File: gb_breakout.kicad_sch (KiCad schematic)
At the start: 13 parts, among them J1 Conn_02x16_Counter_Clockwise, U1 Cartridge_Bus

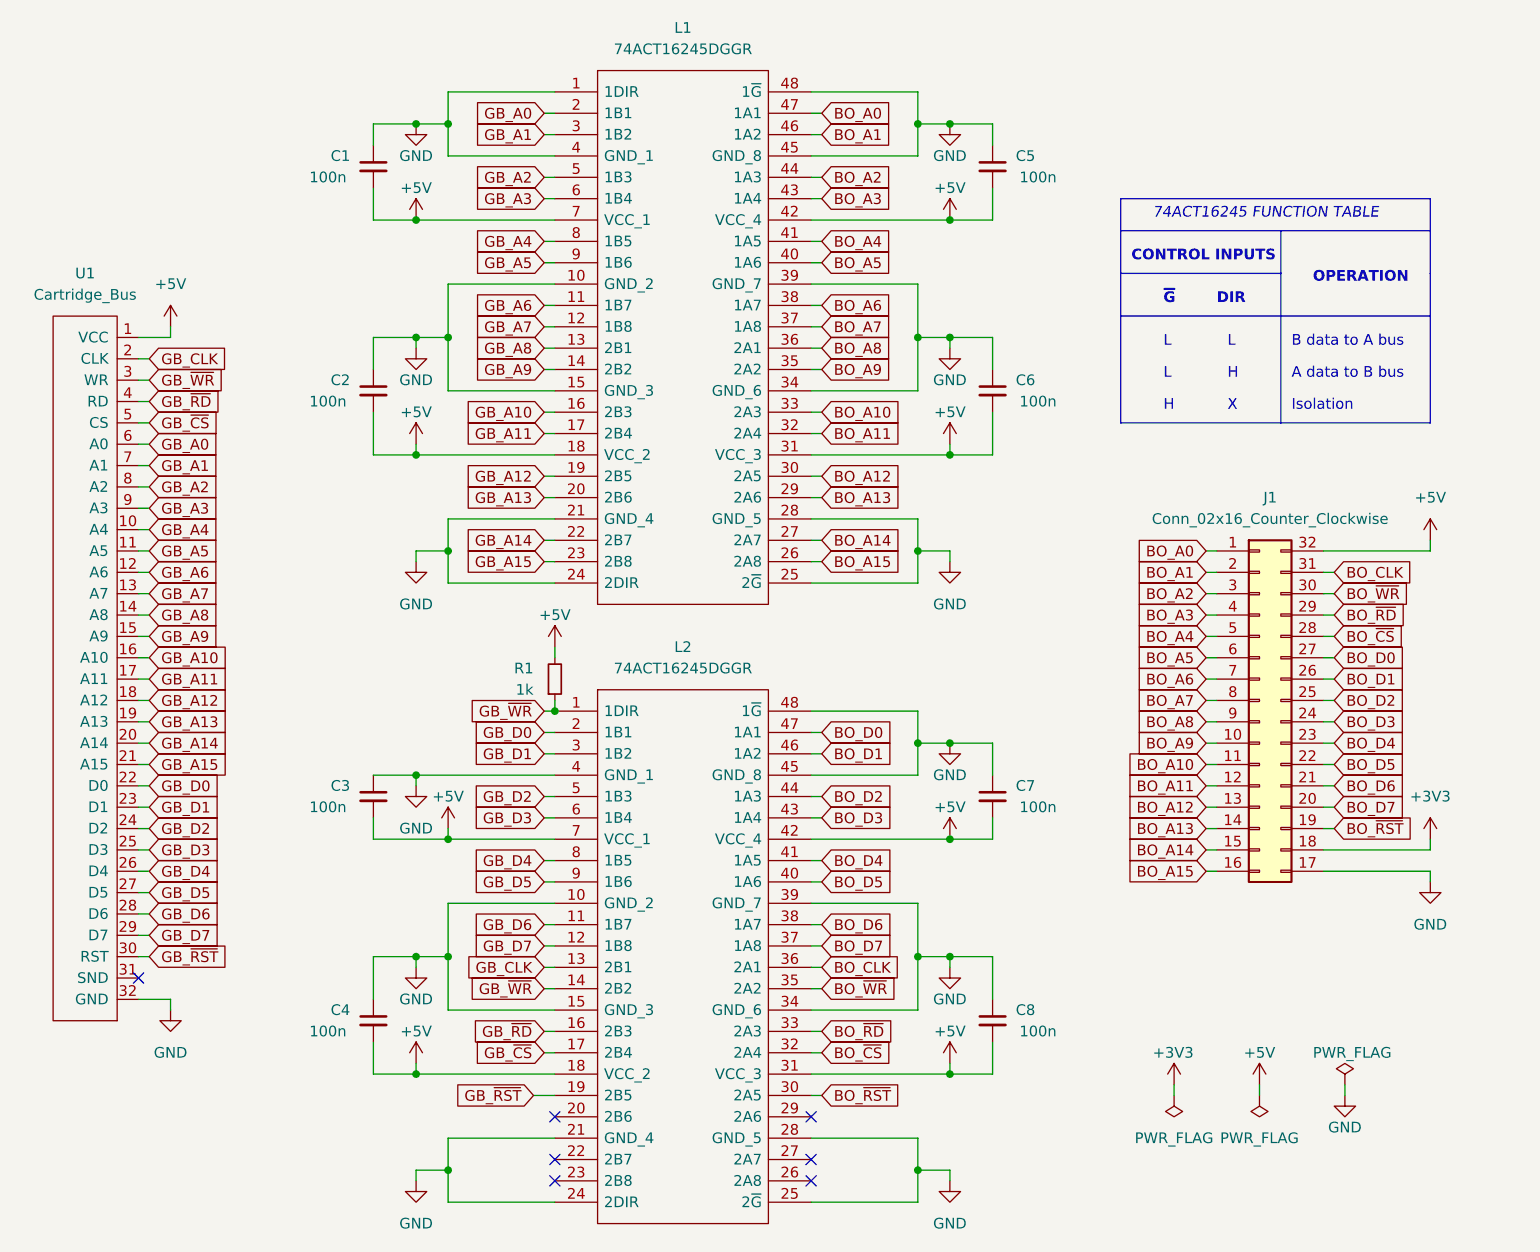
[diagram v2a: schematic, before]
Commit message: switched to 74ALVC164245 for level shifting
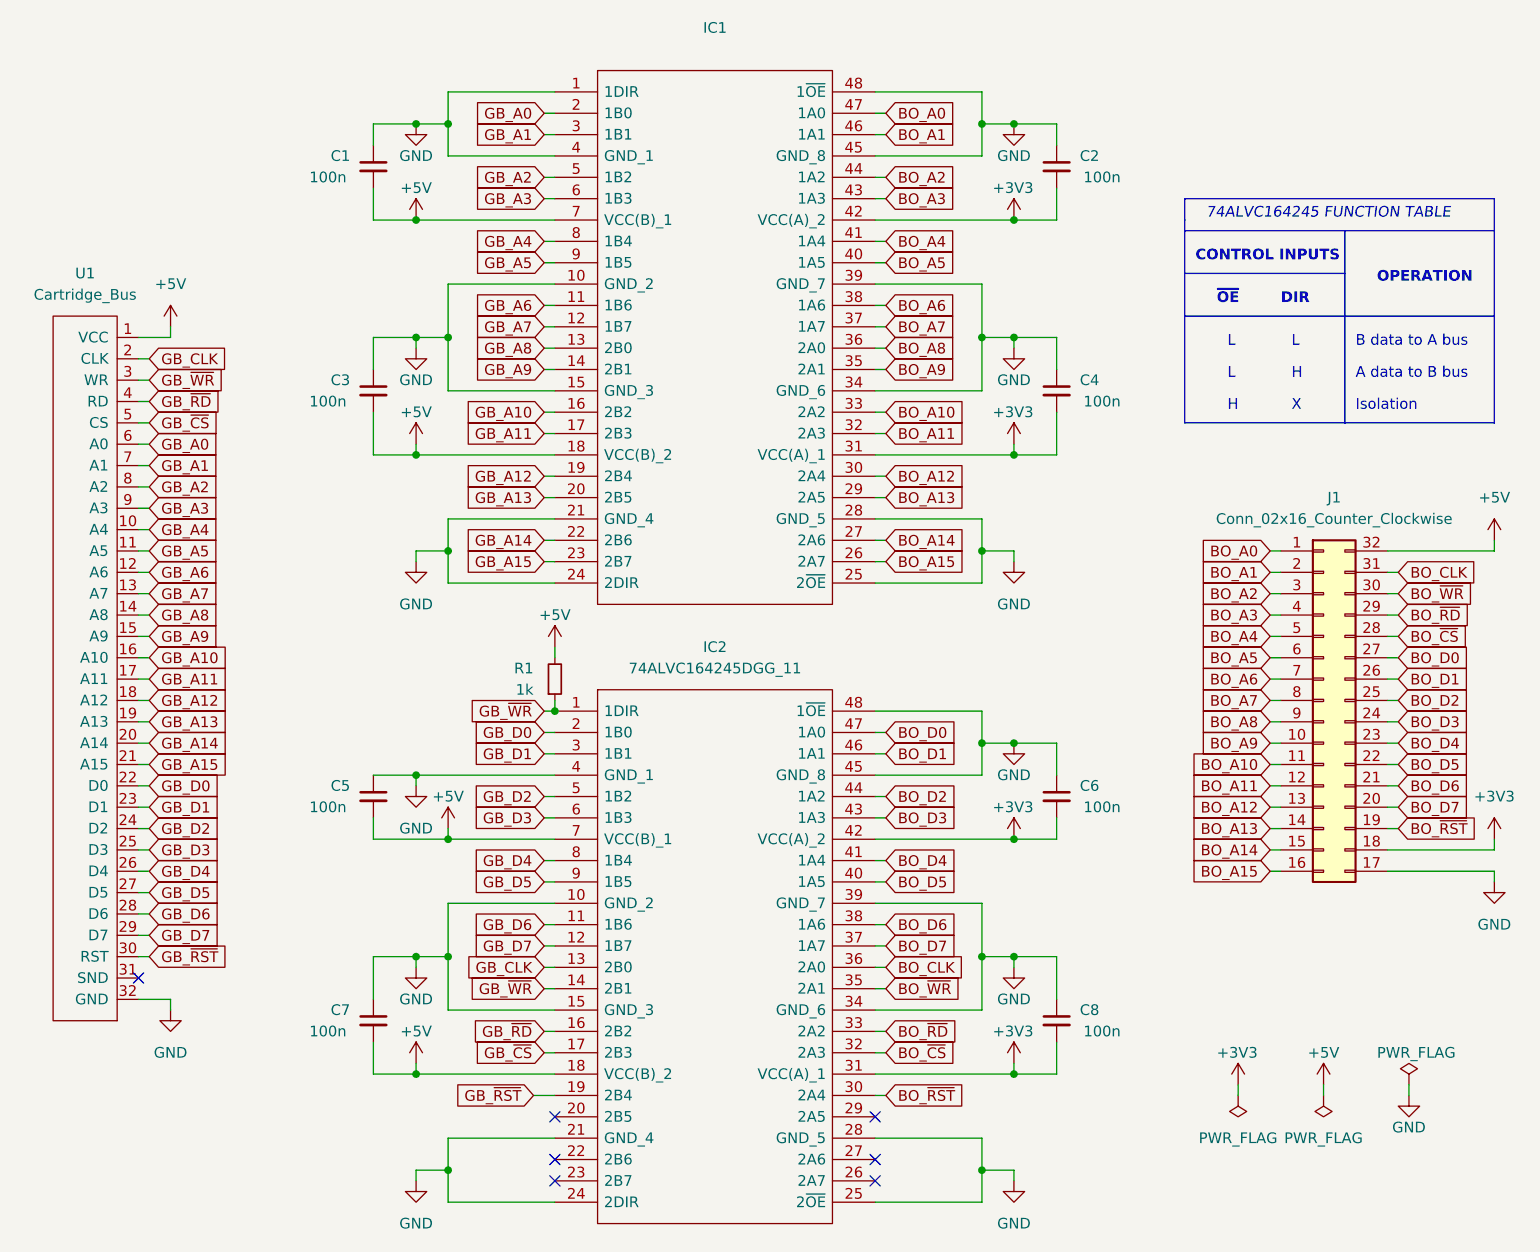
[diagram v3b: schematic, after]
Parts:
- removed L1, L2: 74ACT16245DGGR, 74ACT16245DGGR:SOP50P810X120-48N, symbol 74ACT16245DGGR:74ACT16245DGGR
- added IC1: (no value), symbol 74ALVC164245DGG_11:74ALVC164245DGG_11
- added IC2: 74ALVC164245DGG_11, symbol 74ALVC164245DGG_11:74ALVC164245DGG_11
- renumbered C5 to C2, C2 to C3, C6 to C4, C3 to C5, C7 to C6, C4 to C7
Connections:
- net +3V3: now also C2.2, C4.2, C6.2, C8.2, IC1.31 (VCC(A)_1), IC1.42 (VCC(A)_2), IC2.31 (VCC(A)_1), IC2.42 (VCC(A)_2)
- net +5V: now also IC1.18 (VCC(B)_2), IC1.7 (VCC(B)_1), IC2.18 (VCC(B)_2), IC2.7 (VCC(B)_1); no longer C2.2, C4.2, C6.2, C8.2
- net BO_A0: now also IC1.47 (1A0)
- net BO_A1: now also IC1.46 (1A1)
- net BO_A10: now also IC1.33 (2A2)
- net BO_A11: now also IC1.32 (2A3)
- net BO_A12: now also IC1.30 (2A4)
- net BO_A13: now also IC1.29 (2A5)
- net BO_A14: now also IC1.27 (2A6)
- net BO_A15: now also IC1.26 (2A7)
- net BO_A2: now also IC1.44 (1A2)
- net BO_A3: now also IC1.43 (1A3)
- net BO_A4: now also IC1.41 (1A4)
- net BO_A5: now also IC1.40 (1A5)
- net BO_A6: now also IC1.38 (1A6)
- net BO_A7: now also IC1.37 (1A7)
- net BO_A8: now also IC1.36 (2A0)
- net BO_A9: now also IC1.35 (2A1)
- net BO_CLK: now also IC2.36 (2A0)
- net BO_D0: now also IC2.47 (1A0)
- net BO_D1: now also IC2.46 (1A1)
- net BO_D2: now also IC2.44 (1A2)
- net BO_D3: now also IC2.43 (1A3)
- net BO_D4: now also IC2.41 (1A4)
- net BO_D5: now also IC2.40 (1A5)
- net BO_D6: now also IC2.38 (1A6)
- net BO_D7: now also IC2.37 (1A7)
- net BO_~{CS}: now also IC2.32 (2A3)
- net BO_~{RD}: now also IC2.33 (2A2)
- net BO_~{RST}: now also IC2.30 (2A4)
- net BO_~{WR}: now also IC2.35 (2A1)
- net GB_A0: now also IC1.2 (1B0)
- net GB_A1: now also IC1.3 (1B1)
- net GB_A10: now also IC1.16 (2B2)
- net GB_A11: now also IC1.17 (2B3)
- net GB_A12: now also IC1.19 (2B4)
- net GB_A13: now also IC1.20 (2B5)
- net GB_A14: now also IC1.22 (2B6)
- net GB_A15: now also IC1.23 (2B7)
- net GB_A2: now also IC1.5 (1B2)
- net GB_A3: now also IC1.6 (1B3)
- net GB_A4: now also IC1.8 (1B4)
- net GB_A5: now also IC1.9 (1B5)
- net GB_A6: now also IC1.11 (1B6)
- net GB_A7: now also IC1.12 (1B7)
- net GB_A8: now also IC1.13 (2B0)
- net GB_A9: now also IC1.14 (2B1)
- net GB_CLK: now also IC2.13 (2B0)
- net GB_D0: now also IC2.2 (1B0)
- net GB_D1: now also IC2.3 (1B1)
- net GB_D2: now also IC2.5 (1B2)
- net GB_D3: now also IC2.6 (1B3)
- net GB_D4: now also IC2.8 (1B4)
- net GB_D5: now also IC2.9 (1B5)
- net GB_D6: now also IC2.11 (1B6)
- net GB_D7: now also IC2.12 (1B7)
- net GB_~{CS}: now also IC2.17 (2B3)
- net GB_~{RD}: now also IC2.16 (2B2)
- net GB_~{RST}: now also IC2.19 (2B4)
- net GB_~{WR}: now also IC2.1 (1DIR), IC2.14 (2B1)
- net GND: now also IC1.1 (1DIR), IC1.10 (GND_2), IC1.15 (GND_3), IC1.21 (GND_4), IC1.24 (2DIR), IC1.25 (2~{OE}), IC1.28 (GND_5), IC1.34 (GND_6), IC1.39 (GND_7), IC1.4 (GND_1), IC1.45 (GND_8), IC1.48 (1~{OE}), IC2.10 (GND_2), IC2.15 (GND_3), IC2.21 (GND_4), IC2.24 (2DIR), IC2.25 (2~{OE}), IC2.28 (GND_5), IC2.34 (GND_6), IC2.39 (GND_7), IC2.4 (GND_1), IC2.45 (GND_8), IC2.48 (1~{OE})
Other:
- note added: "74ALVC164245 FUNCTION TABLE"
- note added: "~{OE}"
- note removed: "74ACT16245 FUNCTION TABLE"
- note removed: "~{G}"
- moved on the sheet: C2, C4, C6, C8, J1

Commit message: finish routing address lines, start routing data lines
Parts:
- IC1: value (none) -> 74ALVC164245DGG_11; footprint (none) -> 74ALVC164245DGG_11:SOP50P810X120-48N
- IC2: footprint (none) -> 74ALVC164245DGG_11:SOP50P810X120-48N
- U1: value Cartridge_Bus -> (none); footprint HDR_Gameboy_Cartridges:GB_Cartridge -> (none)
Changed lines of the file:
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@@
     (in_bom yes) (on_board yes) (fields_autoplaced)
     (property "Reference" "IC1" (id 0) (at 135.89 16.51 0))
-    (property "Value" "" (id 1) (at 135.89 19.05 0))
-    (property "Footprint" "" (id 2) (at 151.13 21.59 0)
+    (property "Value" "74ALVC164245DGG_11" (id 1) (at 135.89 19.05 0))
+    (property "Footprint" "74ALVC164245DGG_11:SOP50P810X120-48N" (id 2) (at 151.13 21.59 0)
       (effects (font (size 1.27 1.27)) (justify left) hide)
     )
@@
     (property "Reference" "IC2" (id 0) (at 135.89 90.17 0))
     (property "Value" "74ALVC164245DGG_11" (id 1) (at 135.89 92.71 0))
-    (property "Footprint" "" (id 2) (at 151.13 95.25 0)
+    (property "Footprint" "74ALVC164245DGG_11:SOP50P810X120-48N" (id 2) (at 151.13 95.25 0)
       (effects (font (size 1.27 1.27)) (justify left) hide)
     )
@@
     (in_bom yes) (on_board yes) (fields_autoplaced)
     (property "Reference" "U1" (id 0) (at 60.96 45.72 90))
-    (property "Value" "Cartridge_Bus" (id 1) (at 60.96 48.26 90))
-    (property "Footprint" "HDR_Gameboy_Cartridges:GB_Cartridge" (id 2) (at 64.77 68.58 0)
+    (property "Value" "" (id 1) (at 60.96 48.26 90))
+    (property "Footprint" "" (id 2) (at 64.77 68.58 0)
       (effects (font (size 1.27 1.27)) hide)
     )
@@
       (reference "R1") (unit 1) (value "1k") (footprint "Resistor_SMD:R_0201_0603Metric")
     )
-    (path "/85255a37-874d-44ab-bbc7-86e671be0f3c"
+    (path "/8445dacb-1773-4653-87d7-55d6d433fe85"
       (reference "U1") (unit 1) (value "Cartridge_Bus") (footprint "HDR_Gameboy_Cartridges:GB_Cartridge")
     )

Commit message: switch decoupling caps to imperial 0603
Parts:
- C1, C2, C3, C4, C5, C6, C7, C8: footprint Capacitor_SMD:C_0201_0603Metric -> (none)
- U1: value (none) -> Cartridge_Bus; footprint (none) -> HDR_Gameboy_Cartridges:GB_Cartridge
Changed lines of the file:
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@@
       (effects (font (size 1.27 1.27)) (justify right))
     )
-    (property "Footprint" "Capacitor_SMD:C_0201_0603Metric" (id 2) (at 95.25 134.62 0)
+    (property "Footprint" "" (id 2) (at 95.25 134.62 0)
       (effects (font (size 1.27 1.27)) hide)
     )
@@
     (in_bom yes) (on_board yes) (fields_autoplaced)
     (property "Reference" "U1" (id 0) (at 60.96 45.72 90))
-    (property "Value" "" (id 1) (at 60.96 48.26 90))
-    (property "Footprint" "" (id 2) (at 64.77 68.58 0)
+    (property "Value" "Cartridge_Bus" (id 1) (at 60.96 48.26 90))
+    (property "Footprint" "HDR_Gameboy_Cartridges:GB_Cartridge" (id 2) (at 64.77 68.58 0)
       (effects (font (size 1.27 1.27)) hide)
     )
@@
       (effects (font (size 1.27 1.27)) (justify right))
     )
-    (property "Footprint" "Capacitor_SMD:C_0201_0603Metric" (id 2) (at 176.53 107.95 0)
+    (property "Footprint" "" (id 2) (at 176.53 107.95 0)
       (effects (font (size 1.27 1.27)) hide)
     )
@@
       (effects (font (size 1.27 1.27)) (justify right))
     )
-    (property "Footprint" "Capacitor_SMD:C_0201_0603Metric" (id 2) (at 95.25 33.02 0)
+    (property "Footprint" "" (id 2) (at 95.25 33.02 0)
       (effects (font (size 1.27 1.27)) hide)
     )
@@
       (effects (font (size 1.27 1.27)) (justify right))
     )
-    (property "Footprint" "Capacitor_SMD:C_0201_0603Metric" (id 2) (at 176.53 33.02 0)
+    (property "Footprint" "" (id 2) (at 176.53 33.02 0)
       (effects (font (size 1.27 1.27)) hide)
     )
@@
       (effects (font (size 1.27 1.27)) (justify right))
     )
-    (property "Footprint" "Capacitor_SMD:C_0201_0603Metric" (id 2) (at 95.25 107.95 0)
+    (property "Footprint" "" (id 2) (at 95.25 107.95 0)
       (effects (font (size 1.27 1.27)) hide)
     )
@@
       (effects (font (size 1.27 1.27)) (justify right))
     )
-    (property "Footprint" "Capacitor_SMD:C_0201_0603Metric" (id 2) (at 95.25 59.69 0)
+    (property "Footprint" "" (id 2) (at 95.25 59.69 0)
       (effects (font (size 1.27 1.27)) hide)
     )
@@
       (effects (font (size 1.27 1.27)) (justify right))
     )
-    (property "Footprint" "Capacitor_SMD:C_0201_0603Metric" (id 2) (at 176.53 134.62 0)
+    (property "Footprint" "" (id 2) (at 176.53 134.62 0)
       (effects (font (size 1.27 1.27)) hide)
     )
@@
       (effects (font (size 1.27 1.27)) (justify right))
     )
-    (property "Footprint" "Capacitor_SMD:C_0201_0603Metric" (id 2) (at 176.53 59.69 0)
+    (property "Footprint" "" (id 2) (at 176.53 59.69 0)
       (effects (font (size 1.27 1.27)) hide)
     )
@@
     )
     (path "/b28ab19b-bca4-4c48-a58e-b5d9af57f72a"
-      (reference "C1") (unit 1) (value "100n") (footprint "Capacitor_SMD:C_0201_0603Metric")
+      (reference "C1") (unit 1) (value "100n") (footprint "Capacitor_SMD:C_0603_1608Metric")
     )
     (path "/c1c79e97-1af4-44e8-8145-8598afcefda6"
-      (reference "C2") (unit 1) (value "100n") (footprint "Capacitor_SMD:C_0201_0603Metric")
+      (reference "C2") (unit 1) (value "100n") (footprint "Capacitor_SMD:C_0603_1608Metric")
     )
     (path "/d7fdbe9e-1700-4cf5-a245-374cf5c421c4"
-      (reference "C3") (unit 1) (value "100n") (footprint "Capacitor_SMD:C_0201_0603Metric")
+      (reference "C3") (unit 1) (value "100n") (footprint "Capacitor_SMD:C_0603_1608Metric")
     )
     (path "/eaf44118-1c97-4a04-bd08-7f5f3930e3c3"
-      (reference "C4") (unit 1) (value "100n") (footprint "Capacitor_SMD:C_0201_0603Metric")
+      (reference "C4") (unit 1) (value "100n") (footprint "Capacitor_SMD:C_0603_1608Metric")
     )
     (path "/c72ef019-ae6c-480c-92b2-d4acdb88f1b4"
-      (reference "C5") (unit 1) (value "100n") (footprint "Capacitor_SMD:C_0201_0603Metric")
+      (reference "C5") (unit 1) (value "100n") (footprint "Capacitor_SMD:C_0603_1608Metric")
     )
     (path "/a0c04f80-50ce-4686-9cd8-3561acf71cdf"
-      (reference "C6") (unit 1) (value "100n") (footprint "Capacitor_SMD:C_0201_0603Metric")
+      (reference "C6") (unit 1) (value "100n") (footprint "Capacitor_SMD:C_0603_1608Metric")
     )
     (path "/45d4dd6f-89e1-4931-ba6e-054a4fe7705f"
-      (reference "C7") (unit 1) (value "100n") (footprint "Capacitor_SMD:C_0201_0603Metric")
+      (reference "C7") (unit 1) (value "100n") (footprint "Capacitor_SMD:C_0603_1608Metric")
     )
     (path "/e882b0ad-ca30-4e2e-939a-5215cd594475"
-      (reference "C8") (unit 1) (value "100n") (footprint "Capacitor_SMD:C_0201_0603Metric")
+      (reference "C8") (unit 1) (value "100n") (footprint "Capacitor_SMD:C_0603_1608Metric")
     )
     (path "/66868d80-e5fb-48b0-9aba-6c8277e8b027"

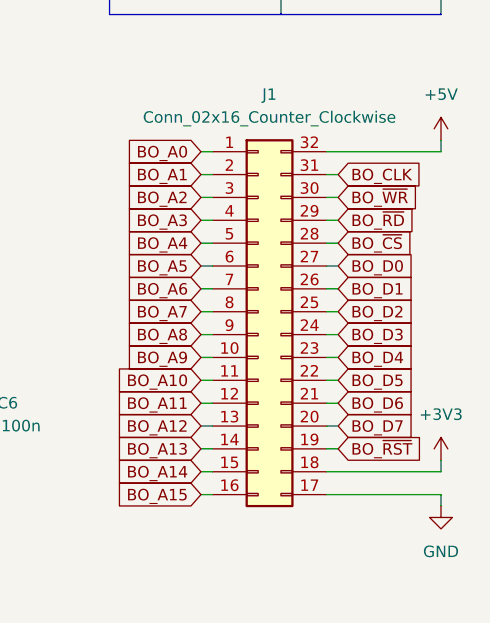
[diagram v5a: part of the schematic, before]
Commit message: fix pin header pinout to make better sense to route
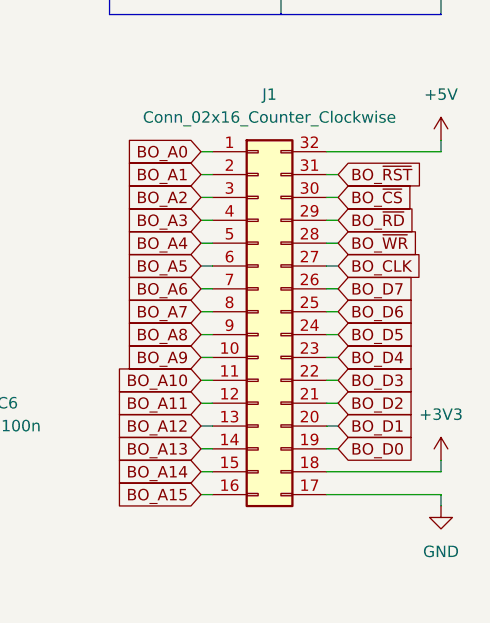
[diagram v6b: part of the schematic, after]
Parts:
- C1, C2, C3, C4, C5, C6, C7, C8: footprint (none) -> Capacitor_SMD:C_0603_1608Metric
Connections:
- net BO_CLK: now also J1.27 (Pin_27); no longer J1.31 (Pin_31)
- net BO_D0: now also J1.19 (Pin_19); no longer J1.27 (Pin_27)
- net BO_D1: now also J1.20 (Pin_20); no longer J1.26 (Pin_26)
- net BO_D2: now also J1.21 (Pin_21); no longer J1.25 (Pin_25)
- net BO_D3: now also J1.22 (Pin_22); no longer J1.24 (Pin_24)
- net BO_D5: now also J1.24 (Pin_24); no longer J1.22 (Pin_22)
- net BO_D6: now also J1.25 (Pin_25); no longer J1.21 (Pin_21)
- net BO_D7: now also J1.26 (Pin_26); no longer J1.20 (Pin_20)
- net BO_~{CS}: now also J1.30 (Pin_30); no longer J1.28 (Pin_28)
- net BO_~{RST}: now also J1.31 (Pin_31); no longer J1.19 (Pin_19)
- net BO_~{WR}: now also J1.28 (Pin_28); no longer J1.30 (Pin_30)

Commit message: change 0201 resistor to 0402, woops
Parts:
- R1: footprint Resistor_SMD:R_0201_0603Metric -> (none)
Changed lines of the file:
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@@
       (effects (font (size 1.27 1.27)) (justify right))
     )
-    (property "Footprint" "Resistor_SMD:R_0201_0603Metric" (id 2) (at 116.84 93.98 0)
+    (property "Footprint" "" (id 2) (at 116.84 93.98 0)
       (effects (font (size 1.27 1.27)) hide)
     )
@@
     )
     (path "/6a0e53e1-b857-43dc-a42e-67e035257304"
-      (reference "R1") (unit 1) (value "1k") (footprint "Resistor_SMD:R_0201_0603Metric")
+      (reference "R1") (unit 1) (value "1k") (footprint "Resistor_SMD:R_0402_1005Metric")
     )
     (path "/8445dacb-1773-4653-87d7-55d6d433fe85"

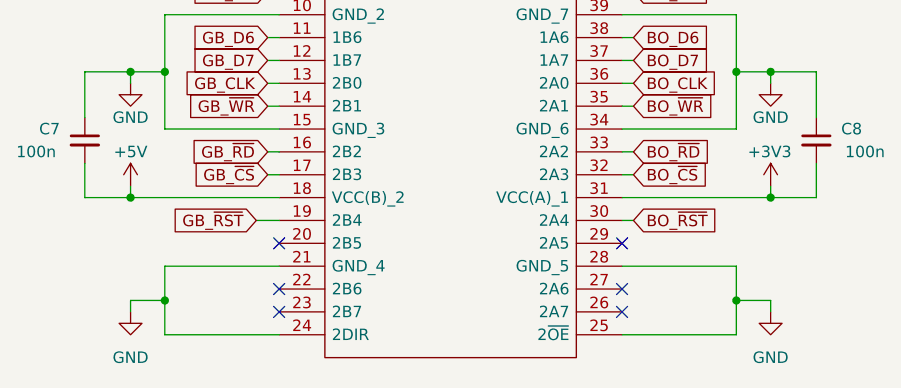
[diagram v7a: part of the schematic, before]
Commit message: add pulldown resistors to floating transciever pins, update render, update BOM
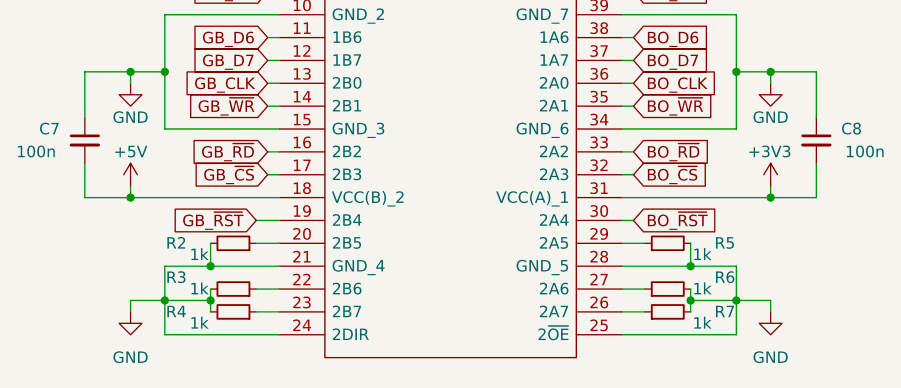
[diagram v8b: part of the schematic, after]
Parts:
- added R2, R3, R4, R5, R6, R7: 1k, Resistor_SMD:R_0402_1005Metric, symbol Device:R_Small
- R1: footprint (none) -> Resistor_SMD:R_0402_1005Metric
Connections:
- net GND: now also R2.2, R3.2, R4.2, R5.2, R6.2, R7.2
- net at IC2.20 (2B5): now also R2.1
- net at IC2.22 (2B6): now also R3.1
- net at IC2.23 (2B7): now also R4.1
- net at IC2.26 (2A7): now also R7.1
- net at IC2.27 (2A6): now also R6.1
- net at IC2.29 (2A5): now also R5.1
- no-connect marks 7 -> 1
